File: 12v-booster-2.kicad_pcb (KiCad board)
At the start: 2 copper layers, 36.7 x 16.9 mm, 23 parts, among them J1 Conn_01x06, J2 Conn_01x06, Q1 BSS214NW, Q2 Si4421DY, U1 TPS611781RNW

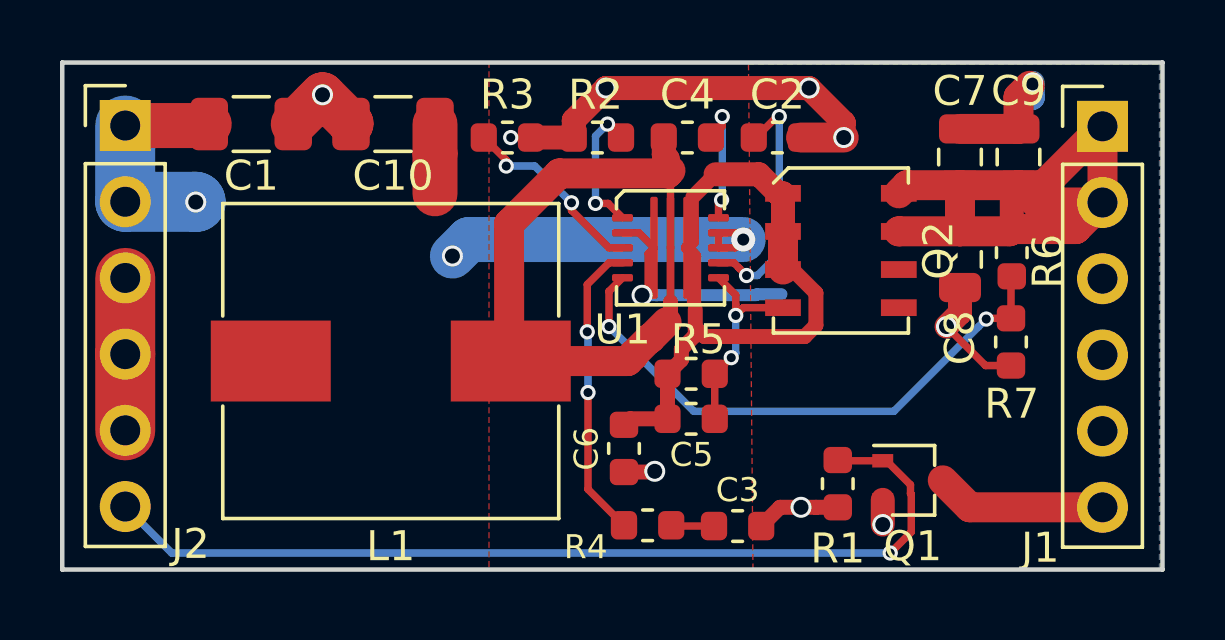
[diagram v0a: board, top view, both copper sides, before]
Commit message: Increased output to 2A
Signed-off-by: Aaron Williams <aaron.w2@gmail.com>
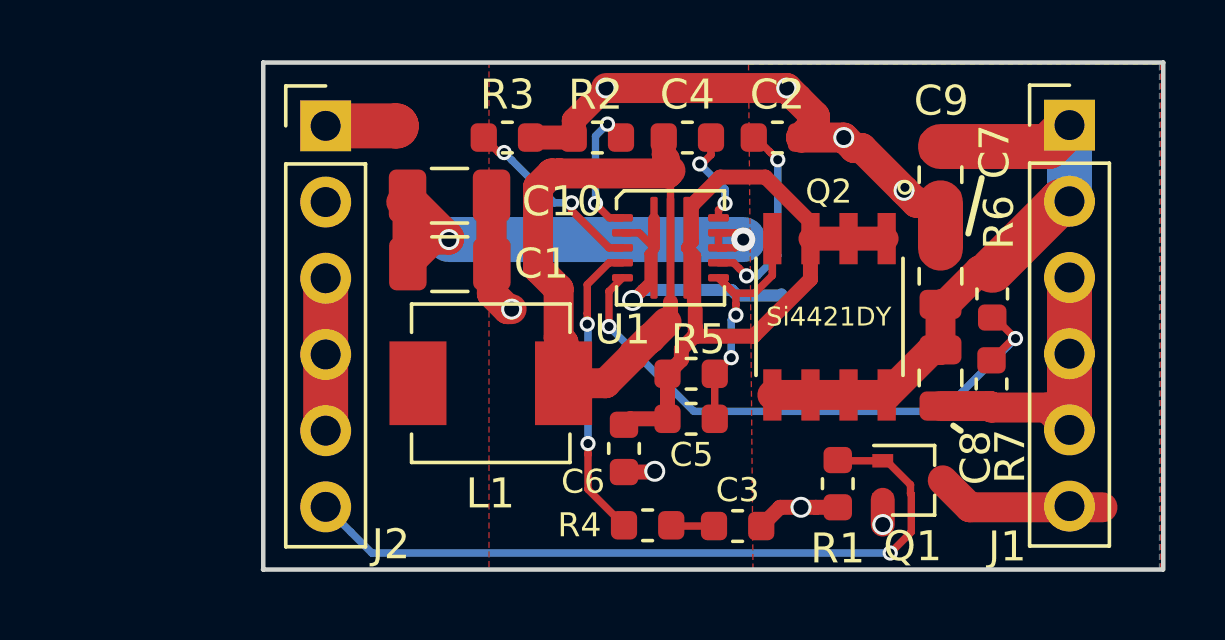
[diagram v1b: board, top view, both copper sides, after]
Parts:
- C3: value 1000pF -> 680pF
- L1: value 1.3uH -> 0.068uH; footprint Aaron:L_Coilcraft_MLC1250 -> Inductor_SMD:L_Vishay_IHLP-2020
- Q2: footprint Aaron:SO-8_3.9x4.9mm_P1.27mm -> Aaron:SOIC127P600X175-8N
- R2: value 86.6K -> 88.7K
- R3: value 73.2K -> 68.1K
- R4: value 47.5K -> 44.2K
- R5: value 154K -> 162K
- moved C1 8.10 mm to (123.1, 66.6)
- moved J2 6.68 mm to (119.0, 62.0)
- moved C7 4.03 mm to (139.5, 67.0)
- moved C8 4.00 mm to (139.5, 70.4)
- moved L1 3.41 mm to (124.5, 70.6)
- moved C10 3.04 mm to (123.1, 64.3), turned to 0 degrees
- moved C9 2.67 mm to (139.5, 63.6), turned to 270 degrees
- moved Q2 2.24 mm to (135.8, 68.4)
- moved R7 1.54 mm to (141.2, 70.6)
- moved R6 1.52 mm to (141.2, 67.6)
- moved J1 1.10 mm to (143.8, 62.0)
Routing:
- net GND: track 43.3 -> 51.9 mm, vias 11 -> 9
- net /PWM_CTL: track 31.5 -> 24.8 mm
- net +12V: track 23.9 -> 20.6 mm
- net /SW: track 24.8 -> 22.2 mm
- net /DISDRV: track 6.92 -> 8.72 mm
- net /VCC: track 8.21 -> 6.69 mm
- net /VOUT: track 24.6 -> 26.0 mm
- net +5V: track 22.3 -> 21.3 mm, vias 3 -> 2
- net /BST: track 4.28 -> 3.31 mm
- net /FB: track 19.1 -> 19.7 mm
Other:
- board size 36.7 x 16.9 mm -> 30 x 16.9 mm
- rule via_min_size: 0.4 -> 0.3
- board text added: "Rev 1.1"
- board text removed: "Rev 1.0"
